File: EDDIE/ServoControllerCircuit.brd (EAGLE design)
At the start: 70.8 x 73.7 mm, 31 parts, among them Q1 20MHz, T1 2N3904, X1 SIGNAL-PWR-GND, X2 SIGNAL-PWR-GND

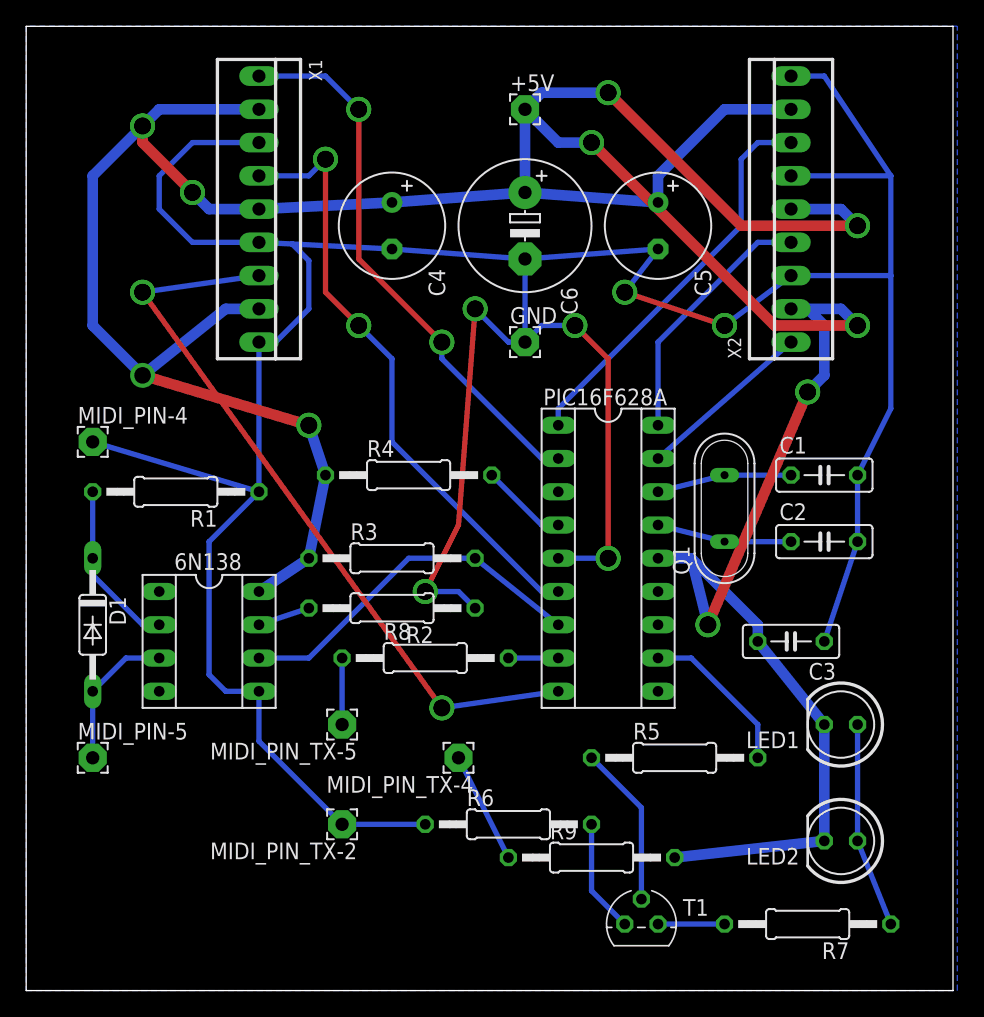
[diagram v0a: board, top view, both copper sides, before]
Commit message: Modified Board Layout for PCB manufacturing
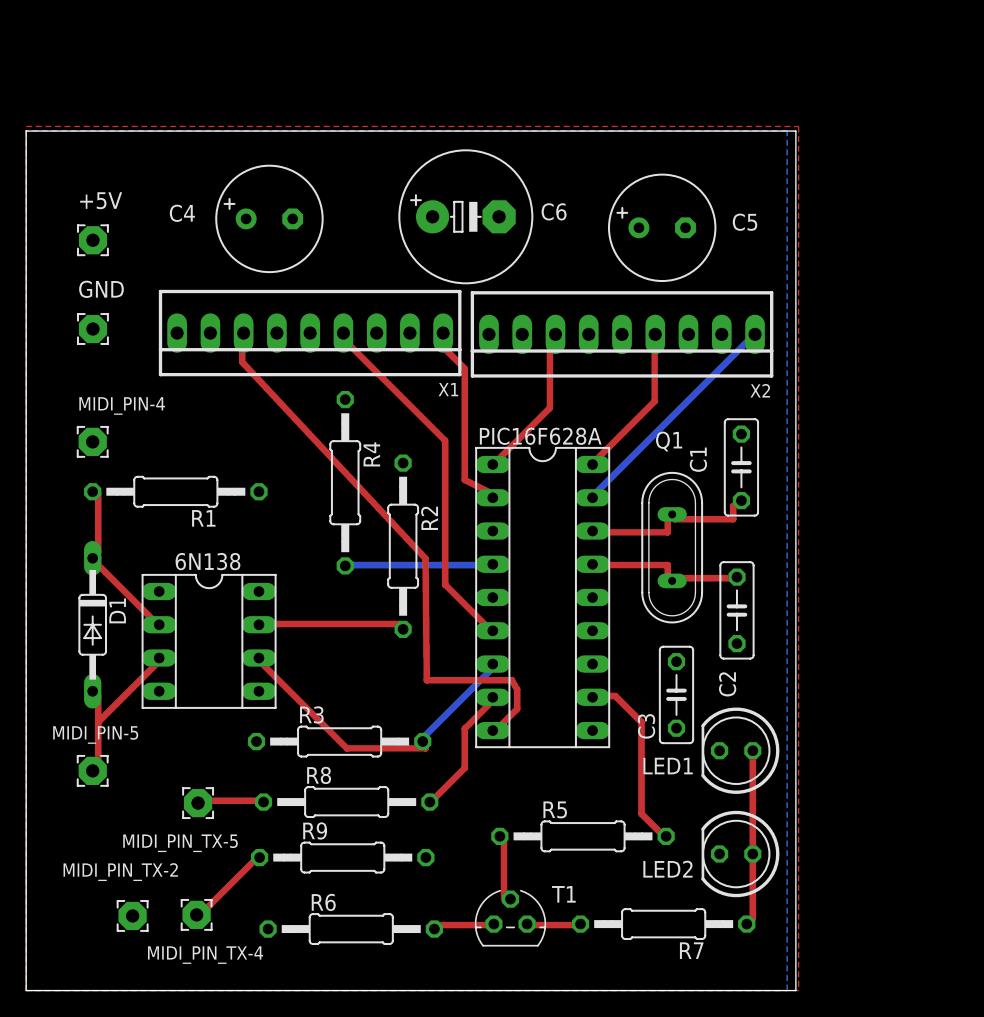
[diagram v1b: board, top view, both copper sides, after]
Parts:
- moved +5V 34.5 mm to (5.10, 57.3)
- moved GND 33.0 mm to (5.10, 50.5)
- moved MIDI_PIN_TX-4 23.3 mm to (13.0, 5.78)
- moved R9 19.0 mm to (24.2, 10.2)
- moved MIDI_PIN_TX-2 17.5 mm to (8.13, 5.70)
- moved X2 16.1 mm to (45.5, 50.1), turned to 180 degrees
- moved R3 14.6 mm to (23.9, 19.0)
- moved R6 14.4 mm to (24.8, 4.70)
- moved MIDI_PIN_TX-5 12.5 mm to (13.1, 14.3)
- moved R8 12.5 mm to (24.5, 14.4)
- moved R7 11.0 mm to (48.7, 5.08)
- moved X1 10.2 mm to (21.7, 50.2), turned to 180 degrees
- moved T1 10.0 mm to (37.0, 5.08)
- moved C3 9.66 mm to (49.7, 22.6), turned to 90 degrees
- moved C4 9.37 mm to (18.6, 58.9), turned to 0 degrees
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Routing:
- net +5V: track 280.9 -> 0.00 mm, vias 10 -> 0
- net GND: track 271.3 -> 0.00 mm, vias 6 -> 0
- net SERVO4: track 42.4 -> 14.5 mm, vias 2 -> 0
- net SERVO5: track 46.7 -> 27.5 mm, vias 2 -> 0
- net SERVO3: track 30.4 -> 12.1 mm
- net SERVO6: track 57.1 -> 43.4 mm, vias 2 -> 0
- net SERVO2: track 19.7 -> 11.9 mm
- net N$2: track 4.02 -> 11.2 mm
- net N$5: track 12.4 -> 5.42 mm
- net TX_PIN: track 3.81 -> 9.98 mm
- net N$6: track 6.66 -> 11.3 mm
- net SERVO1: track 13.5 -> 17.6 mm
- net N$7: track 8.67 -> 4.67 mm
- net N$3: track 10.3 -> 13.9 mm
- net RX_PIN: track 27.8 -> 24.4 mm
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- added copper zone on layer 1, net +5V
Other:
- board size 70.8 x 73.7 mm -> 58.8 x 65.7 mm
